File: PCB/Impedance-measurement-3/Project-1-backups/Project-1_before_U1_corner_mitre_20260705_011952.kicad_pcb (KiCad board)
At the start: 2 copper layers, 171 x 114 mm, 73 parts, among them U1 STM32F303CCT6

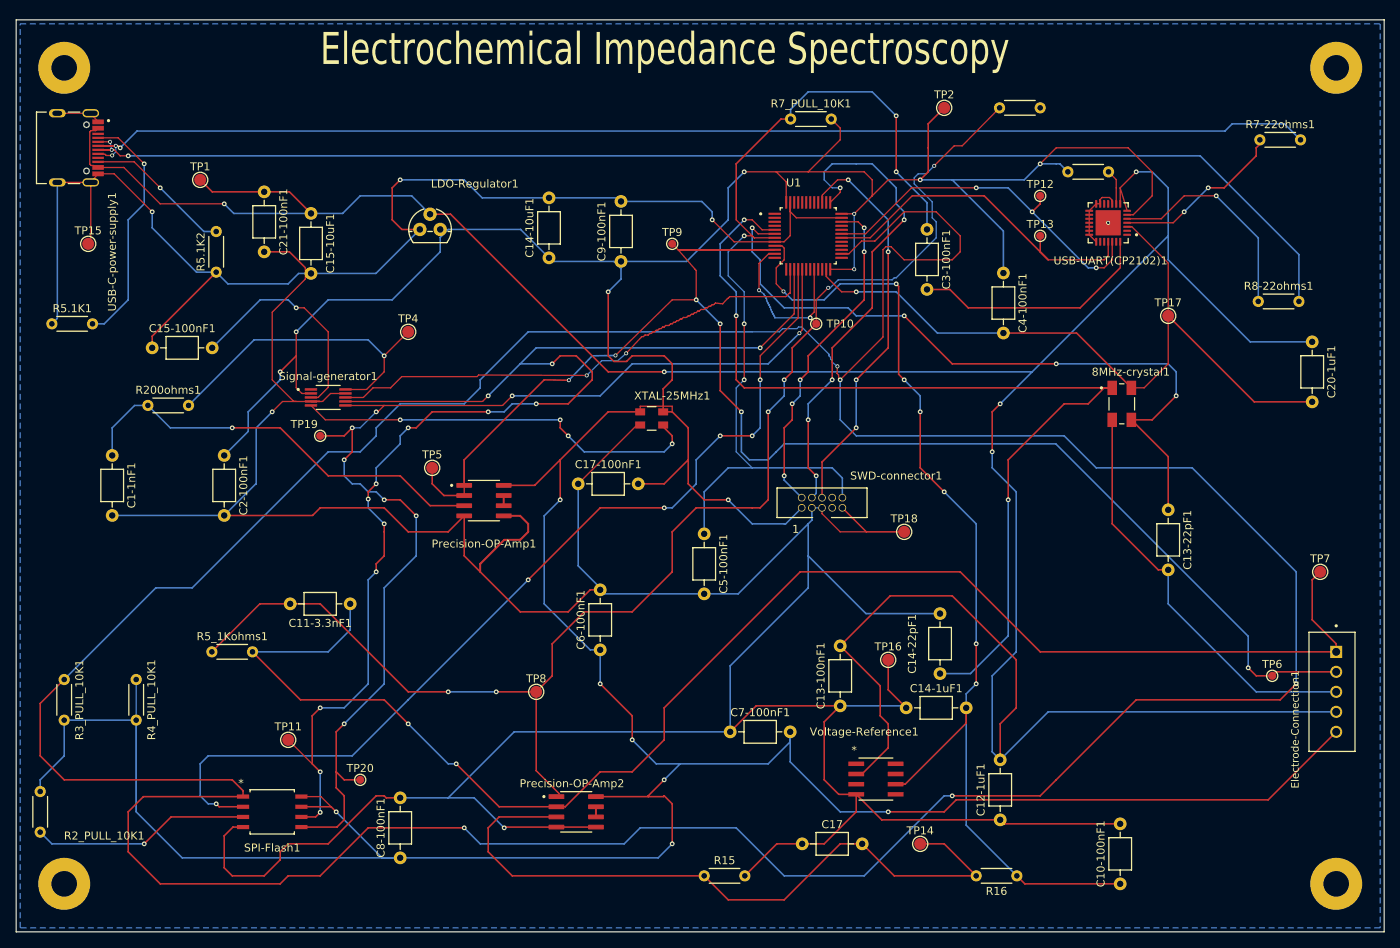
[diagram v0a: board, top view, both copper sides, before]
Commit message: mounting holes included 6/7/2026
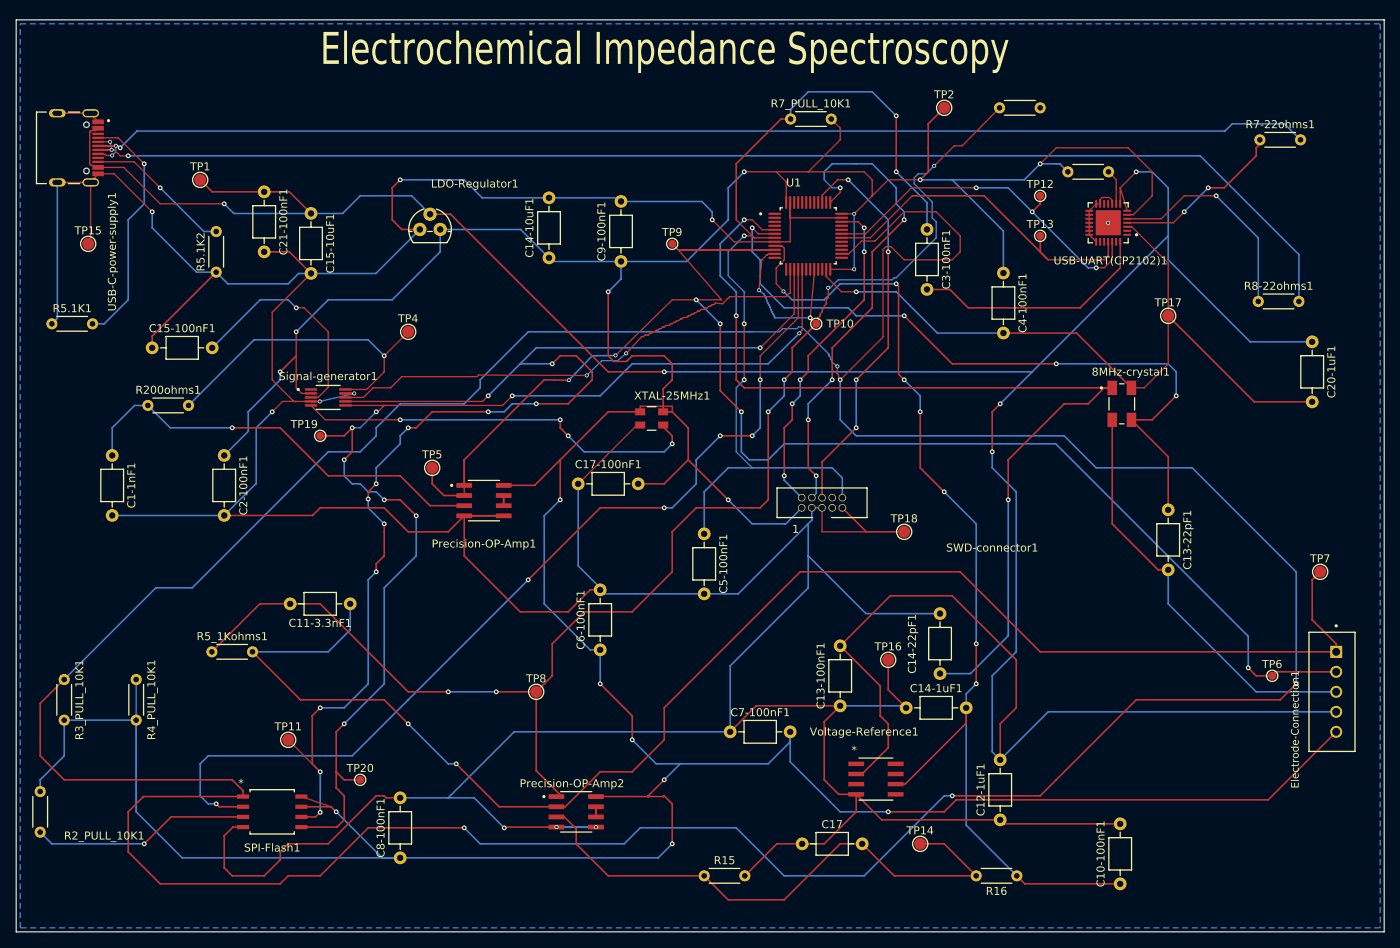
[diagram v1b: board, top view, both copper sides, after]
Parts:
- removed REF** (x4): MountingHole_3.2mm_M3_Pad, MountingHole:MountingHole_3.2mm_M3_Pad
- renumbered R25_PULL_10K1 to R25_PULL_10K
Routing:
- net Net-(C17-Pad2): track 88.8 -> 71.1 mm
- net GND: track 780.0 -> 775.5 mm, vias 7 -> 11
- net /Electrode1: track 195.3 -> 199.7 mm
- net VDD: track 606.4 -> 605.4 mm
